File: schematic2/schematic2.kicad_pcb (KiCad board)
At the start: 2 copper layers, 68.8 x 56 mm, 51 parts, among them J1 Barrel_Jack, K1 TIANBO_HJR_1-2C, P1 Conn_02x20_Odd_Even, Q1 BC547, Q2 DMP1045U, Q3 BC547, Q4 BC547, Q5 BC547, U1 buck, U2 DS3231M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

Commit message: Remove un-needed FET.
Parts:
- removed Q2: DMP1045U, Package_TO_SOT_SMD:SOT-23
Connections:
- K1 pad 13: Net-(K1-Pad13) -> Net-(D7-Pad1)
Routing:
- net Net-(K1-Pad13): track 19.8 -> 0.00 mm
- net Net-(D7-Pad1): track 9.38 -> 21.4 mm
- net +9V: track 87.4 -> 78.7 mm

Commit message: Boards ordered.
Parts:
- added J2: Conn_01x02, Connector_Molex:Molex_KK-254_AE-6410-02A_1x02_P2.54mm_Vertical, F.Cu at (219.1, 113.2)
- added R16: 1K, Resistor_THT:R_Axial_DIN0204_L3.6mm_D1.6mm_P5.08mm_Horizontal, F.Cu at (222.9, 102.4)
- moved C2 2.46 mm to (202.5, 107.5)
- moved U2 1.85 mm to (211.0, 108.6)
- moved D15 1.57 mm to (203.2, 116.1)
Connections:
- net +9V renamed +12V
- K1 pad 11: (no net) -> unconnected-(K1-Pad11)
- K1 pad 4: (no net) -> unconnected-(K1-Pad4)
- K1 pad 6: (no net) -> unconnected-(K1-Pad6)
- K1 pad 8: (no net) -> unconnected-(K1-Pad8)
- P1 pad 10: (no net) -> /GPIO15(RXD0)
- P1 pad 11: (no net) -> GPIO17
- P1 pad 12: (no net) -> /GPIO18(GEN1)(PWM0)
- P1 pad 16: (no net) -> /GPIO23(GEN4)
- P1 pad 17: (no net) -> unconnected-(P1-Pad17)
- P1 pad 18: (no net) -> /GPIO24(GEN5)
- P1 pad 19: (no net) -> /GPIO10(SPI0_MOSI)
- P1 pad 21: (no net) -> /GPIO9(SPI0_MISO)
- P1 pad 22: (no net) -> /GPIO25(GEN6)
- P1 pad 23: (no net) -> /GPIO11(SPI0_SCK)
- P1 pad 24: (no net) -> /GPIO8(SPI0_CE_N)
- P1 pad 26: (no net) -> /GPIO7(SPI1_CE_N)
- P1 pad 27: (no net) -> /ID_SD
- P1 pad 28: (no net) -> /ID_SC
- P1 pad 29: (no net) -> /GPIO5
- P1 pad 31: (no net) -> /GPIO6
- P1 pad 32: (no net) -> /GPIO12(PWM0)
- P1 pad 33: (no net) -> /GPIO13(PWM1)
- P1 pad 35: (no net) -> /GPIO19(SPI1_MISO)
- P1 pad 36: (no net) -> /GPIO16
- P1 pad 37: (no net) -> /GPIO26
- P1 pad 38: (no net) -> /GPIO20(SPI1_MOSI)
- P1 pad 40: (no net) -> /GPIO21(SPI1_SCK)
- P1 pad 7: (no net) -> /GPIO4(GCLK)
- P1 pad 8: (no net) -> /GPIO14(TXD0)
- U2 pad 1: (no net) -> unconnected-(U2-Pad1)
- U2 pad 3: (no net) -> unconnected-(U2-Pad3)
- U2 pad 4: (no net) -> unconnected-(U2-Pad4)
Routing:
- net Net-(J2-Pad2): track 0.00 -> 6.50 mm
- net GPIO17: track 0.00 -> 4.17 mm
- net +3V3: track 28.2 -> 31.8 mm
- net SDA1: track 15.4 -> 13.5 mm
- net CLK_BAT: track 48.1 -> 46.2 mm
- net Net-(BT2-Pad2): track 66.5 -> 64.9 mm
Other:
- net class Bat_Charge removed
- net class Default removed
- net class Power removed

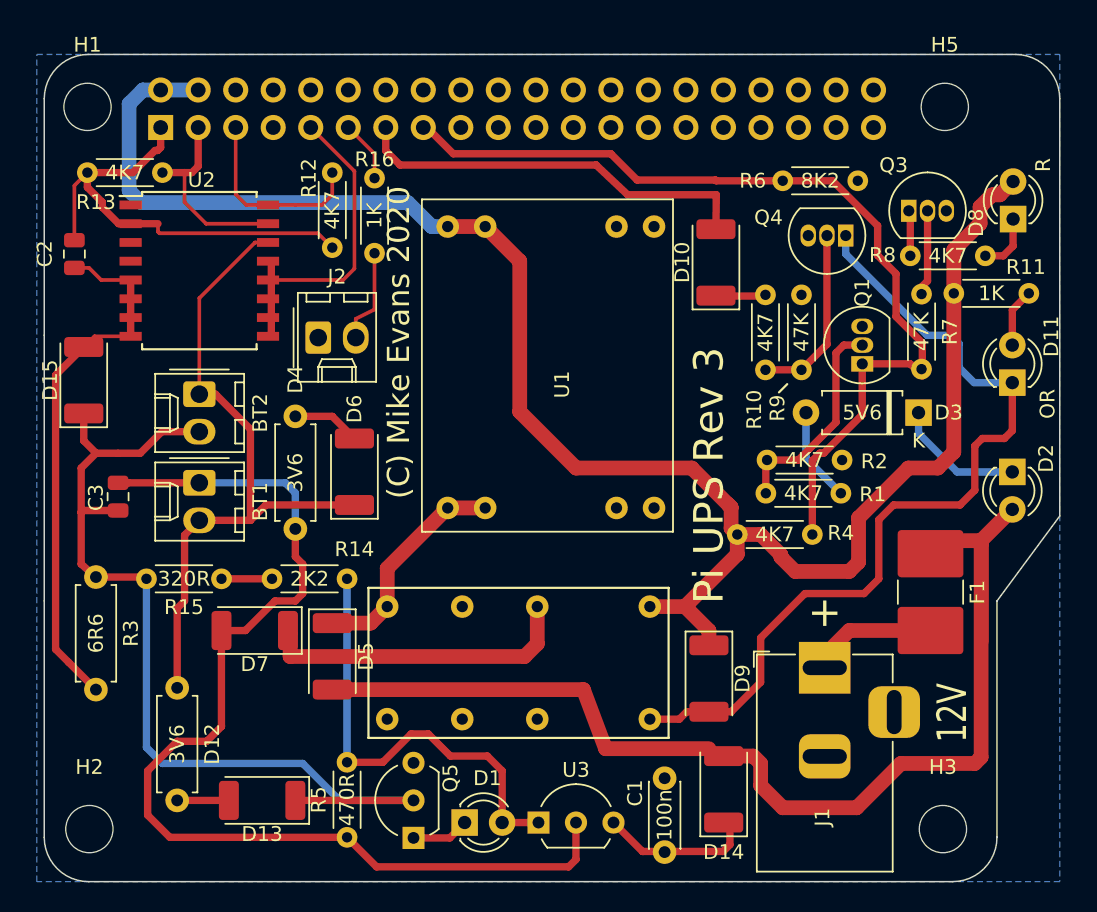
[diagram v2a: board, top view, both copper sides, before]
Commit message: Revert back to KiCAD5
Because the benchy pi cannont run V6.
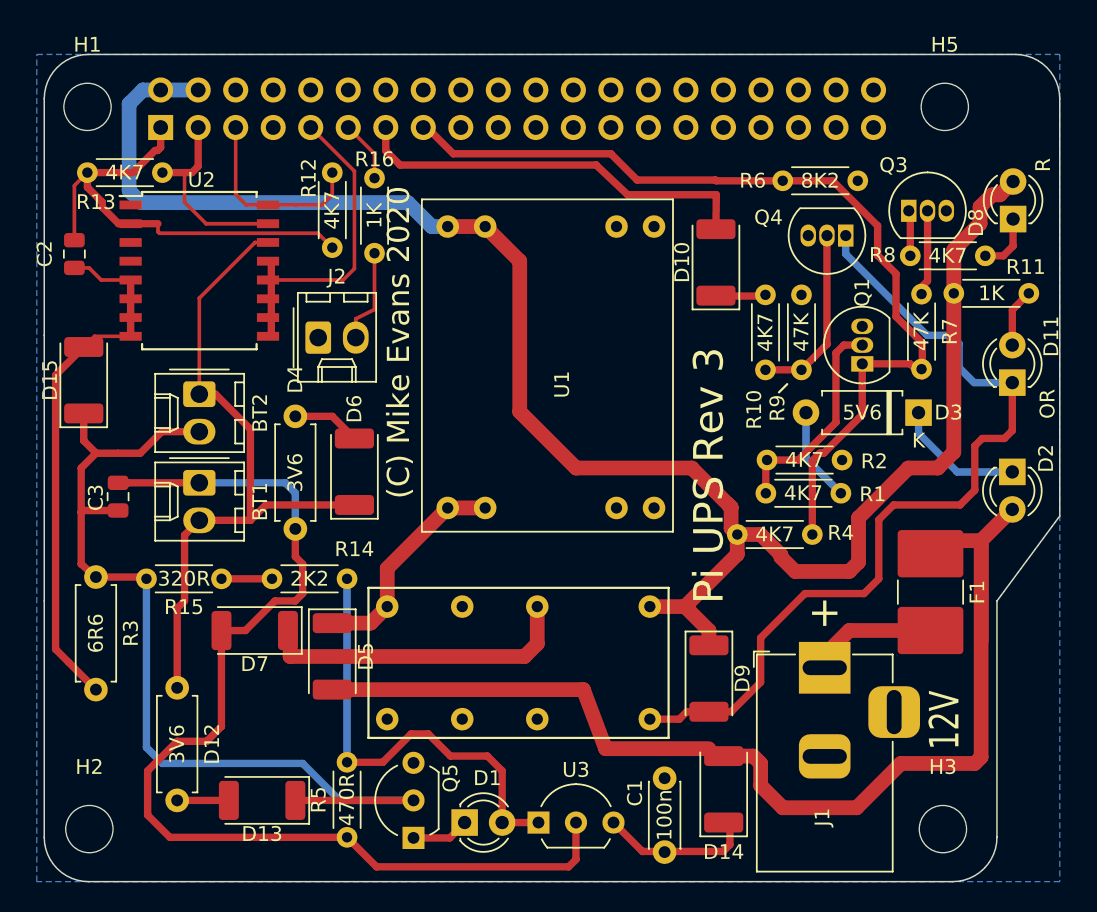
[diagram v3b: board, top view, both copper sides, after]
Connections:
- net +12V renamed +9V
- net GPIO17 renamed BUTTON
- K1 pad 11: unconnected-(K1-Pad11) -> (no net)
- K1 pad 4: unconnected-(K1-Pad4) -> (no net)
- K1 pad 6: unconnected-(K1-Pad6) -> (no net)
- K1 pad 8: unconnected-(K1-Pad8) -> (no net)
- P1 pad 10: /GPIO15(RXD0) -> (no net)
- P1 pad 12: /GPIO18(GEN1)(PWM0) -> (no net)
- P1 pad 16: /GPIO23(GEN4) -> (no net)
- P1 pad 17: unconnected-(P1-Pad17) -> (no net)
- P1 pad 18: /GPIO24(GEN5) -> (no net)
- P1 pad 19: /GPIO10(SPI0_MOSI) -> (no net)
- P1 pad 21: /GPIO9(SPI0_MISO) -> (no net)
- P1 pad 22: /GPIO25(GEN6) -> (no net)
- P1 pad 23: /GPIO11(SPI0_SCK) -> (no net)
- P1 pad 24: /GPIO8(SPI0_CE_N) -> (no net)
- P1 pad 26: /GPIO7(SPI1_CE_N) -> (no net)
- P1 pad 27: /ID_SD -> (no net)
- P1 pad 28: /ID_SC -> (no net)
- P1 pad 29: /GPIO5 -> (no net)
- P1 pad 31: /GPIO6 -> (no net)
- P1 pad 32: /GPIO12(PWM0) -> (no net)
- P1 pad 33: /GPIO13(PWM1) -> (no net)
- P1 pad 35: /GPIO19(SPI1_MISO) -> (no net)
- P1 pad 36: /GPIO16 -> (no net)
- P1 pad 37: /GPIO26 -> (no net)
- P1 pad 38: /GPIO20(SPI1_MOSI) -> (no net)
- P1 pad 40: /GPIO21(SPI1_SCK) -> (no net)
- P1 pad 7: /GPIO4(GCLK) -> (no net)
- P1 pad 8: /GPIO14(TXD0) -> (no net)
- U2 pad 1: unconnected-(U2-Pad1) -> (no net)
- U2 pad 3: unconnected-(U2-Pad3) -> (no net)
- U2 pad 4: unconnected-(U2-Pad4) -> (no net)
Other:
- net class Bat_Charge added: clearance 0.1, trace_width 0.25, via_dia 0.9, via_drill 0.6
- net class Default added: clearance 0.2, trace_width 0.5, via_dia 0.9, via_drill 0.6
- net class Power added: clearance 0.2, trace_width 1, via_dia 1, via_drill 0.7

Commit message: Detail changes made from release note.
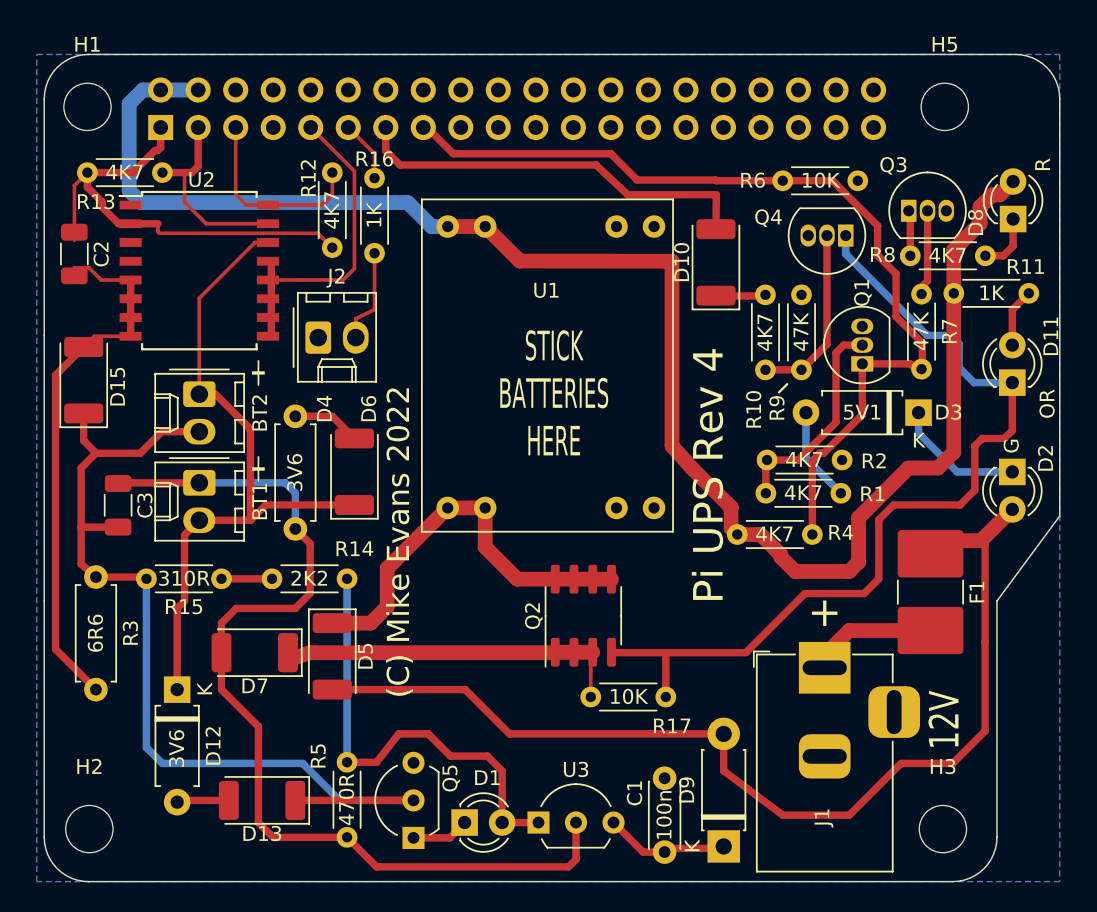
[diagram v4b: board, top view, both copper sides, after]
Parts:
- removed D14: 1N4001, Diode_SMD:D_2010_5025Metric
- removed K1: TIANBO_HJR_1-2C, Mikee:Relay_DPDT_HJR_1-2C
- added Q2: FDS9435A, Package_SO:SOIC-8_3.9x4.9mm_P1.27mm, F.Cu at (237.0, 132.0)
- added R17: 10K, Resistor_THT:R_Axial_DIN0204_L3.6mm_D1.6mm_P5.08mm_Horizontal, F.Cu at (237.5, 137.5)
- BT1, BT2: value Battery_Cell -> 302323 LiPo
- C2, C3: footprint Capacitor_SMD:C_0805_2012Metric -> Capacitor_SMD:C_1206_3216Metric
- D12: footprint Resistor_THT:R_Axial_DIN0207_L6.3mm_D2.5mm_P7.62mm_Horizontal -> Diode_THT:D_A-405_P7.62mm_Horizontal
- D3: value 5V6 -> 5V1
- D9: value 1N4001 -> 1N4148; footprint Diode_SMD:D_2010_5025Metric -> Diode_THT:D_DO-41_SOD81_P7.62mm_Horizontal
- R15: value 320R -> 310R
- R6: value 8K2 -> 10K
- moved D9 11.4 mm to (246.5, 147.6), turned to 90 degrees
- moved D7 1.50 mm to (214.8, 134.5)
- moved C3 0.59 mm to (205.5, 124.5)
- moved D12 0.12 mm to (209.5, 137.0)
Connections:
- net BUTTON renamed GPIO17
- D2 pad 2: +9V -> +12V
- D5 pad 2: +9V -> +12V
- D9 pad 1: +5V -> Net-(C1-Pad1)
- D9 pad 2: Net-(D11-Pad1) -> +12V
- F1 pad 1: +9V -> +12V
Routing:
- net +9V: track 78.7 -> 0.00 mm
- net +12V: track 0.00 -> 71.9 mm
- net Net-(D5-Pad1): track 15.1 -> 27.2 mm
- net +5V: track 122.1 -> 111.4 mm
- net Net-(BT1-Pad1): track 74.7 -> 66.3 mm
- net Net-(D11-Pad1): track 59.3 -> 64.6 mm
- net Net-(C1-Pad1): track 10.6 -> 7.89 mm
- net Net-(D7-Pad1): track 21.4 -> 23.8 mm
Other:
- board text added: "(C) Mike Evans 2022"
- board text added: "Pi UPS Rev 4"
- board text added: "STICK BATTERIES HERE"
- board text removed: "(C) Mike Evans 2020"
- board text removed: "Pi UPS Rev 3"

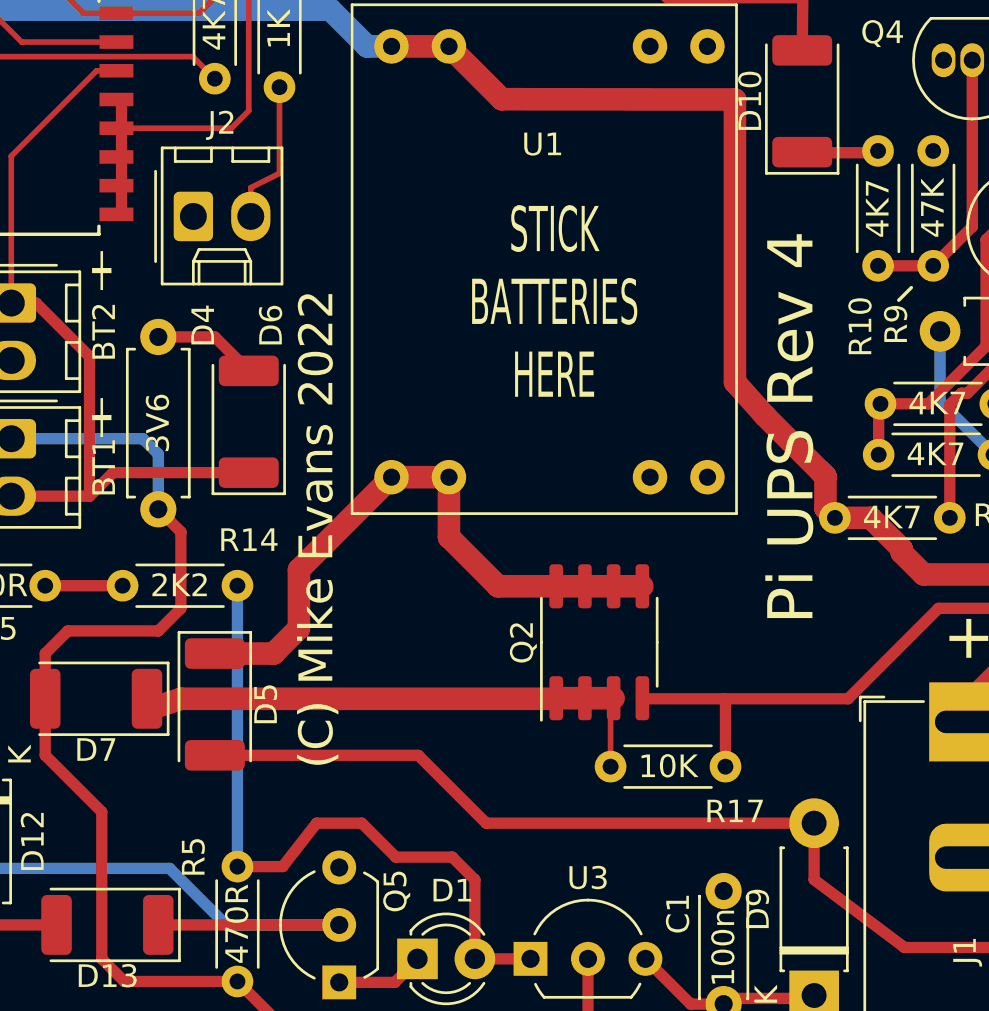
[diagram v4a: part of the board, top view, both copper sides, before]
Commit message: Better view of amended assembly.
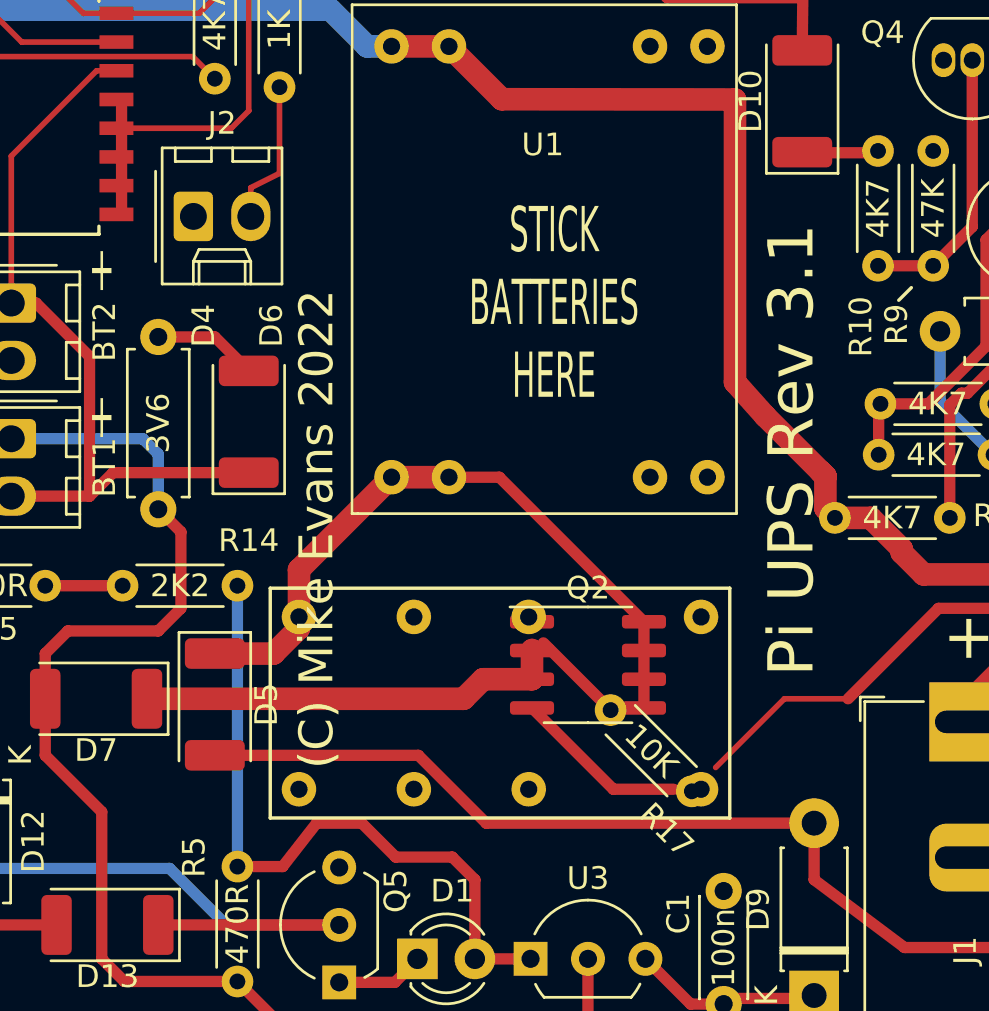
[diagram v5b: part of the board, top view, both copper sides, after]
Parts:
- added K1: TIANBO_HJR_1-2C, Mikee:Relay_DPDT_HJR_1-2C, F.Cu at (241.5, 138.5)
- moved R17 2.50 mm to (237.5, 135.0), turned to 315 degrees
- moved Q2 1.12 mm to (236.5, 133.0), turned to 0 degrees
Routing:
- net Net-(D5-Pad1): track 27.2 -> 30.2 mm
- net Net-(D11-Pad1): track 64.6 -> 63.6 mm
- net Net-(D7-Pad1): track 23.8 -> 23.2 mm
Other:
- board text added: "Pi UPS Rev 3.1"
- board text removed: "Pi UPS Rev 4"
